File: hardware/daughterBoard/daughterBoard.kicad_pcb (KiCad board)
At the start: 4 copper layers, 24 x 36 mm, 46 parts, among them J1 Conn_02x05_Odd_Even, J2 Conn_02x02_Odd_Even, J3 Conn_02x02_Odd_Even, J4 Conn_02x05_Odd_Even, U1 DRV2605LDGSR, U2 TCA9544APWR, U3 VL53L1CXV0FY1, U4 DRV2605LDGSR, U5 IS31FL3193-DLS2-TR

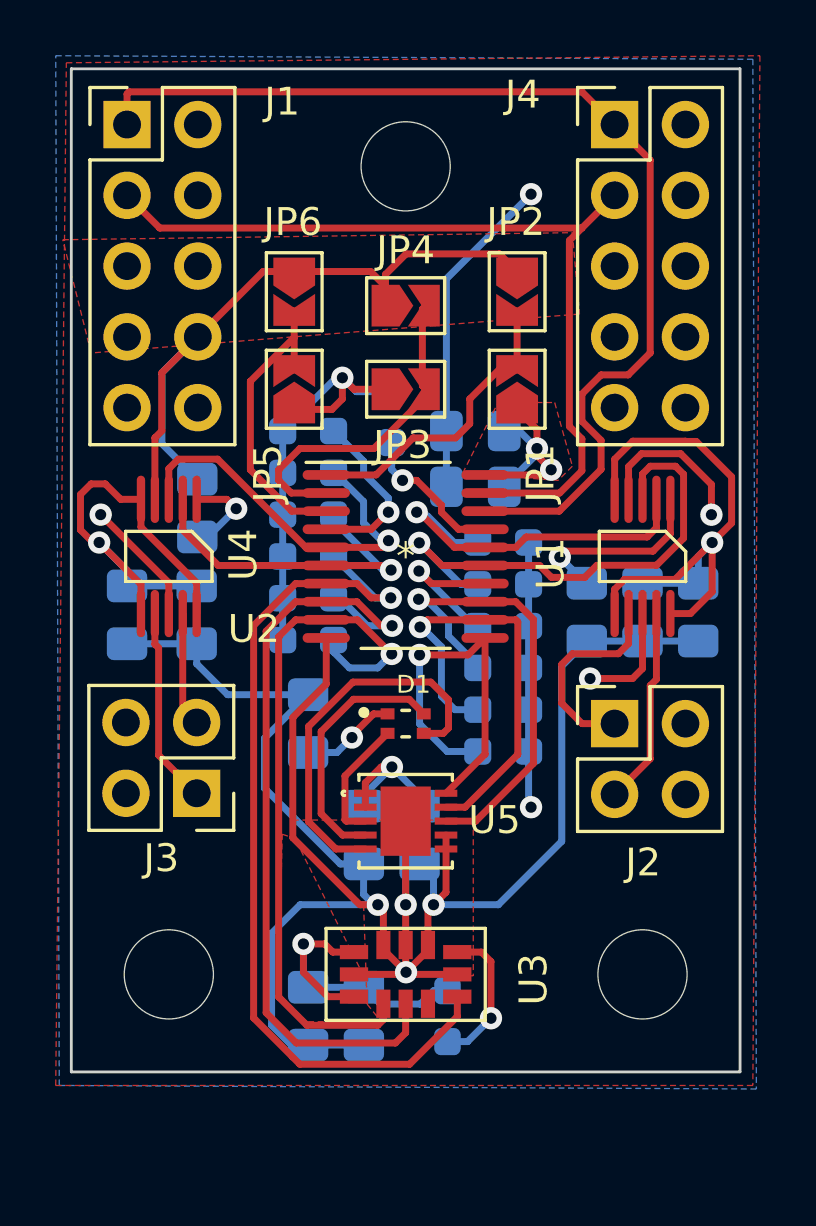
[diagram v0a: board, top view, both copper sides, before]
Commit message: updated board files to rev2
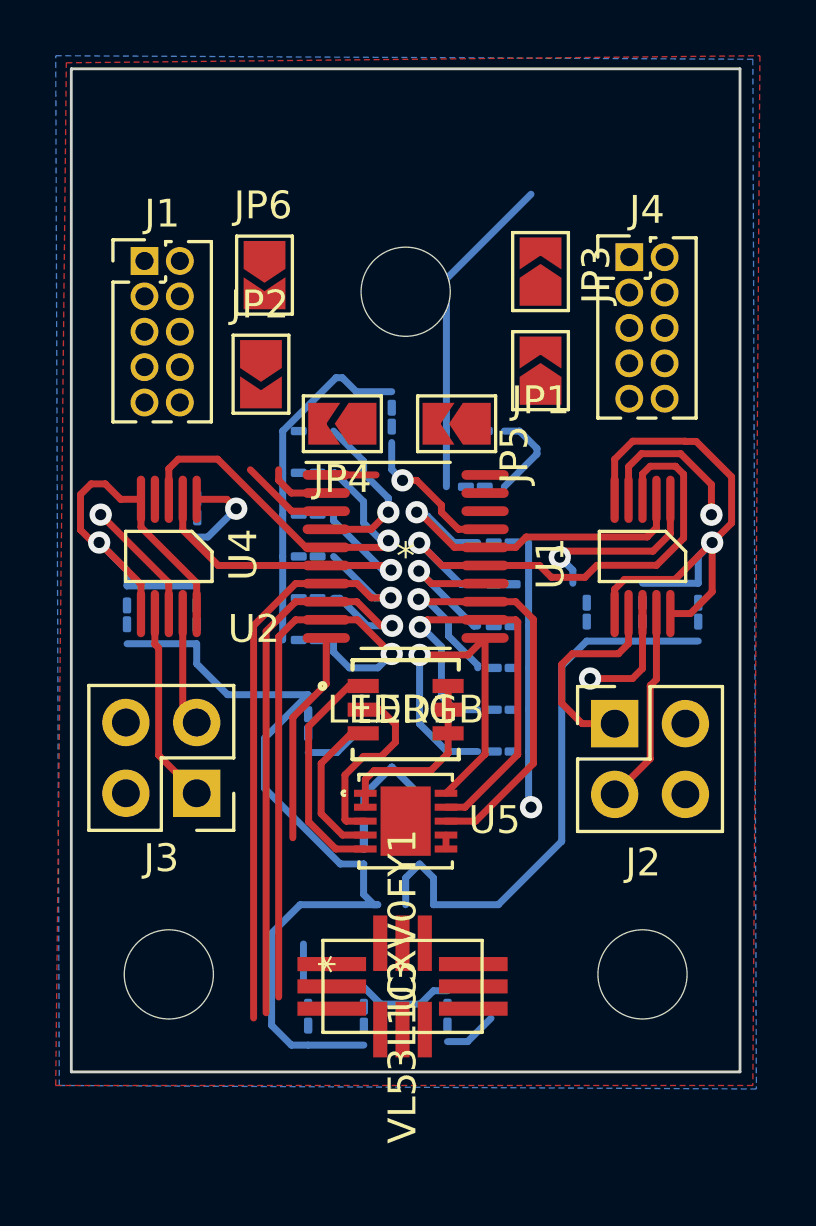
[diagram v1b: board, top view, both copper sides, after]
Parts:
- removed D1: APHF1608LSEEQBDZGKC, LED:LED_APHF1608LSEEQBDZGKC
- added LED1: LEDRGB, LED_New:150352M173300, F.Cu at (112.0, 73.0)
- C1, C10, C11, C12, C13, C2, C3, C4, C5, C6, C7, C9: footprint Capacitor_SMD:C_0805_2012Metric_Pad1.18x1.45mm_HandSolder -> Capacitor_SMD:C_01005_0402Metric_Pad0.57x0.30mm_HandSolder
- C8: value 100n -> .1u; footprint Capacitor_SMD:C_0805_2012Metric_Pad1.18x1.45mm_HandSolder -> Capacitor_SMD:C_01005_0402Metric_Pad0.57x0.30mm_HandSolder
- J1, J4: footprint Connector_PinHeader_2.54mm:PinHeader_2x05_P2.54mm_Vertical -> Connector_PinHeader_1.27mm:PinHeader_2x05_P1.27mm_Vertical
- R1, R10, R11, R12, R13, R14, R2, R3, R4, R5, R6, R7, R8, R9: footprint Resistor_SMD:R_0603_1608Metric_Pad0.98x0.95mm_HandSolder -> Resistor_SMD:R_01005_0402Metric_Pad0.57x0.30mm_HandSolder
- moved JP2 9.66 mm to (106.8, 61.0)
- moved JP5 8.87 mm to (116.8, 60.8)
- moved JP3 6.42 mm to (116.8, 57.3), turned to 90 degrees
- moved J1 4.94 mm to (102.6, 56.9)
- moved JP4 4.81 mm to (109.7, 62.7), turned to 180 degrees
- moved J4 4.79 mm to (120.0, 56.8)
- moved REF** 4.50 mm to (112.0, 58.0)
- moved JP1 2.50 mm to (113.8, 62.7), turned to 180 degrees
- moved JP6 1.22 mm to (106.9, 57.4)
- moved U3 0.45 mm to (111.9, 82.9)
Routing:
- net GND: track 132.9 -> 84.1 mm, vias 8 -> 3
- net /SCM: track 38.7 -> 0.00 mm
- net /SDM: track 31.4 -> 0.00 mm
- net +3V3: track 94.8 -> 83.2 mm, vias 9 -> 3
- net Net-(JP3-Pad2): track 12.0 -> 2.28 mm
- net /INT1: track 31.9 -> 22.5 mm
- net Net-(JP1-Pad2): track 11.0 -> 1.79 mm
- net Net-(JP5-Pad2): track 10.8 -> 3.34 mm
- net /SD1: track 28.2 -> 21.5 mm
- net Net-(U5-Pad5): track 13.8 -> 8.42 mm
- net /SC1: track 25.5 -> 20.7 mm
- net Net-(U5-Pad4): track 9.23 -> 5.66 mm
- net Net-(R1-Pad2): track 5.29 -> 1.91 mm, vias 1 -> 0
- net Net-(U5-Pad3): track 4.49 -> 6.67 mm
- removed copper zone on F.Cu, net +3V3
- removed copper zone on F.Cu, net GND
